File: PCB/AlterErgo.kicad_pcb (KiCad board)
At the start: 2 copper layers, 99 parts, among them J1 GS3, J2 SJ-43514, J3 GS3, SW0:10 SW_Push, SW0:11 SW_Push, SW0:12 SW_Push, SW0:7 SW_Push, SW0:8 SW_Push, SW0:9 SW_Push, SW1 SW_SPST, SW1:10 SW_Push, SW1:11 SW_Push, SW1:12 SW_Push, SW1:13 SW_Push, SW1:9 SW_Push, SW2:10 SW_Push, SW2:11 SW_Push, SW2:12 SW_Push, SW2:13 SW_Push, SW2:7 SW_Push, SW2:8 SW_Push, SW2:9 SW_Push, SW3:10 SW_Push, SW3:11 SW_Push, SW3:12 SW_Push, SW3:13 SW_Push, SW3:8 SW_Push, SW3:9 SW_Push, SW4:10 SW_Push, SW4:11 SW_Push, SW4:12 SW_Push, SW4:13 SW_Push, SW4:7 SW_Push, SW4:8 SW_Push, SW4:9 SW_Push, SW5:10 SW_Push, SW5:11 SW_Push, SW5:12 SW_Push, SW5:13 SW_Push, SW5:7 SW_Push, SW5:8 SW_Push, SW5:9 SW_Push, U1 Feather32u4Bluefruit, U2 MCP23018

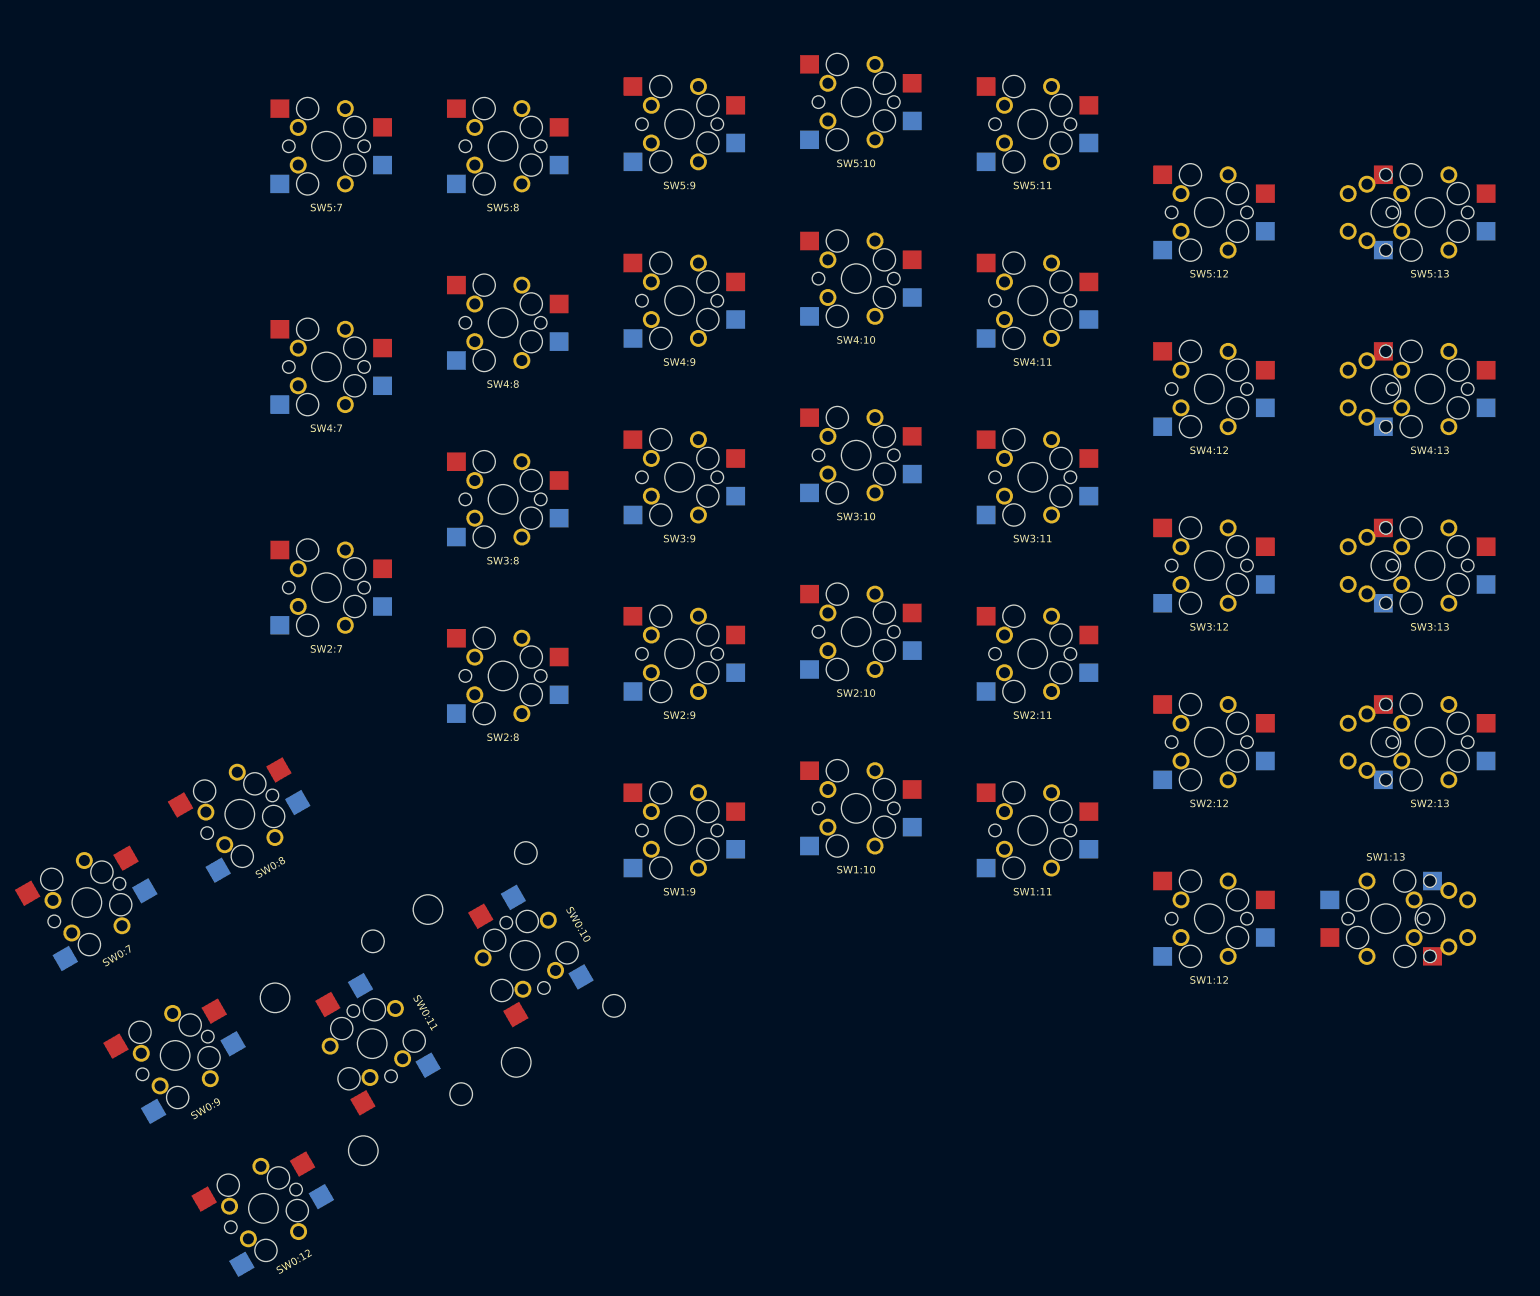
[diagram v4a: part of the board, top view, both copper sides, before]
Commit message: Actually use .75in for key spacing (d'oh!)
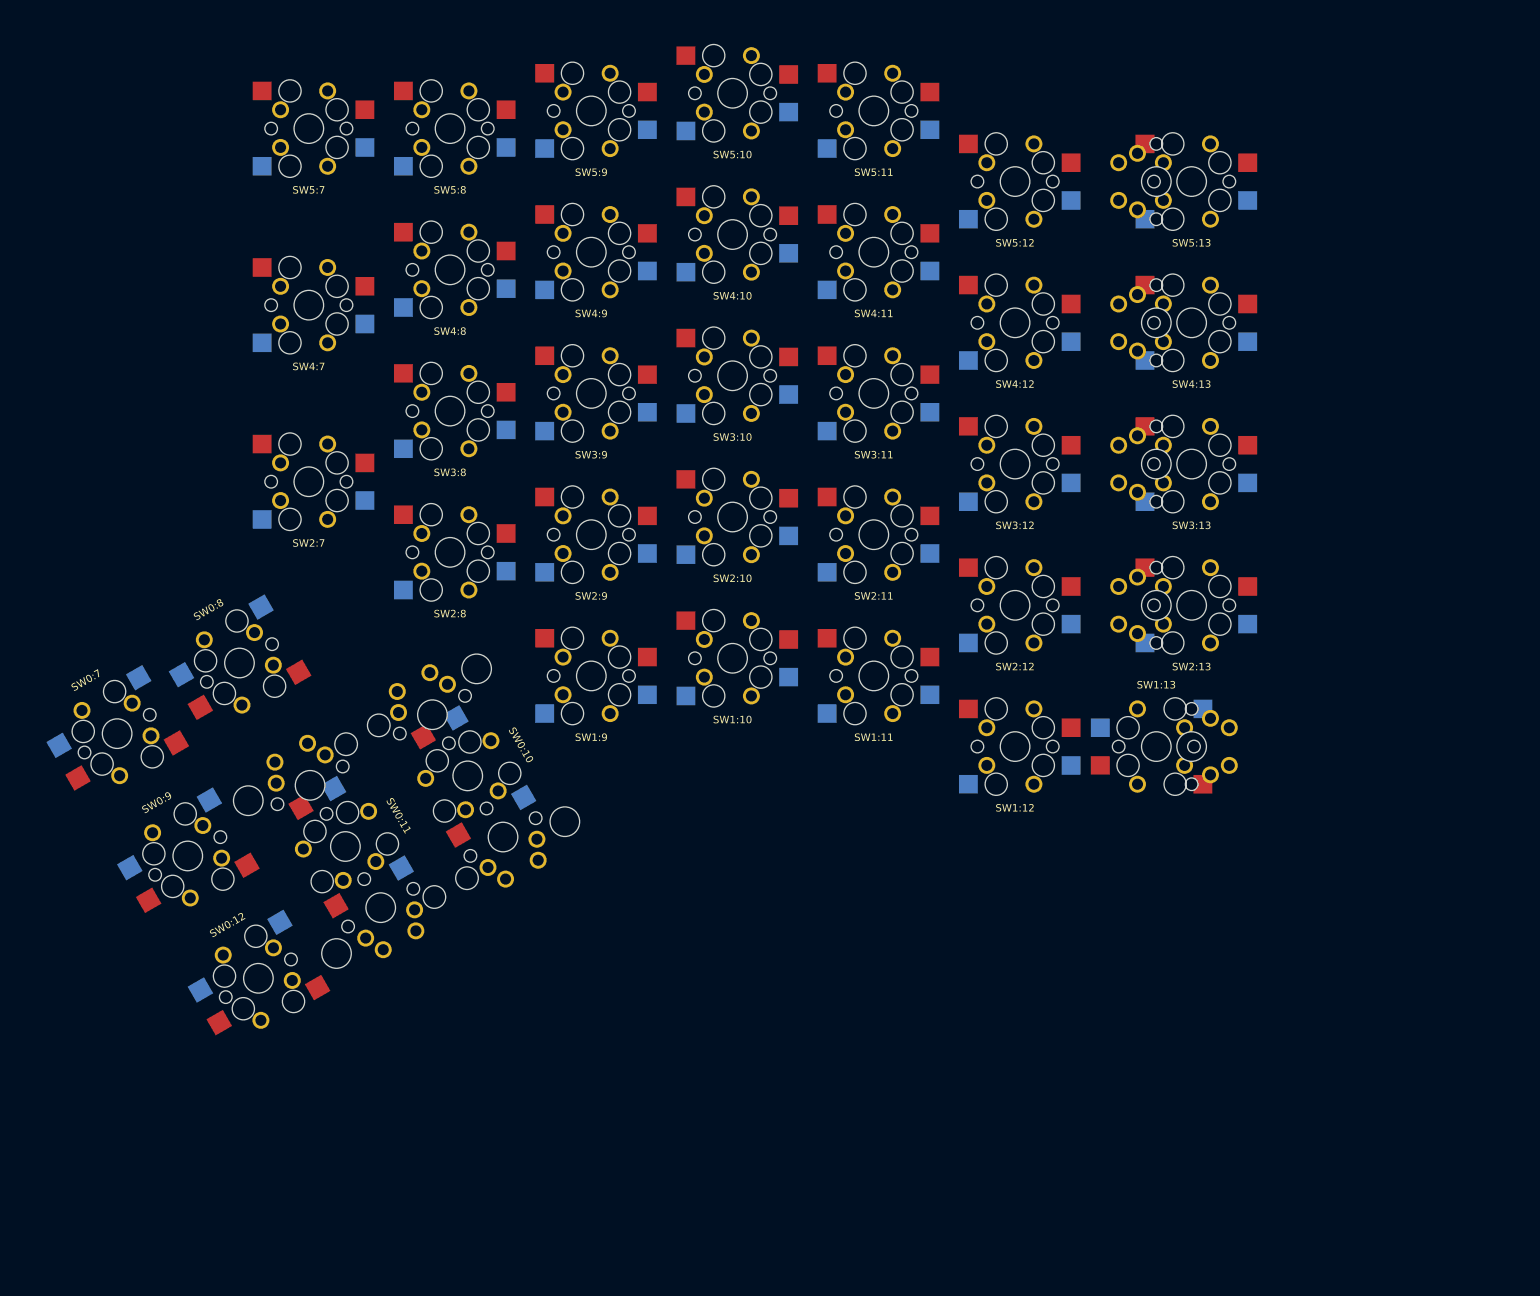
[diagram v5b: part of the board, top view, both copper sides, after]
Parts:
- added SW0:10: SW_Push, keyswitches:MX_reversible, F.Cu at (107.2, 152.7)
- added SW0:11: SW_Push, keyswitches:MX_reversible, F.Cu at (90.7, 162.2)
- added SW1:7: SW_Push, keyswitches:MX_reversible, F.Cu at (81.1, 145.7)
- added SW1:8: SW_Push, keyswitches:MX_reversible, F.Cu at (97.6, 136.2)
- moved ? 39.7 mm to (200.0, 140.5)
- moved SW1:13 38.7 mm to (195.3, 140.5)
- moved SW2:13 37.1 mm to (200.0, 121.4)
- moved ? 36.0 mm to (195.3, 121.4)
- moved SW1:12 35.0 mm to (176.2, 140.5)
- moved SW3:13 34.9 mm to (200.0, 102.4)
- moved ? 33.8 mm to (195.3, 102.4)
- moved SW4:13 33.4 mm to (200.0, 83.3)
- moved SW5:13 32.4 mm to (200.0, 64.3)
- moved ? 32.2 mm to (195.3, 83.3)
- moved SW2:12 32.0 mm to (176.2, 121.4)
- moved ? 31.2 mm to (195.3, 64.3)
- moved SW0:12 31.0 mm to (74.2, 171.7), turned to 210 degrees
- moved SW1:11 29.9 mm to (157.2, 131.0)
- moved SW3:12 29.6 mm to (176.2, 102.4)
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
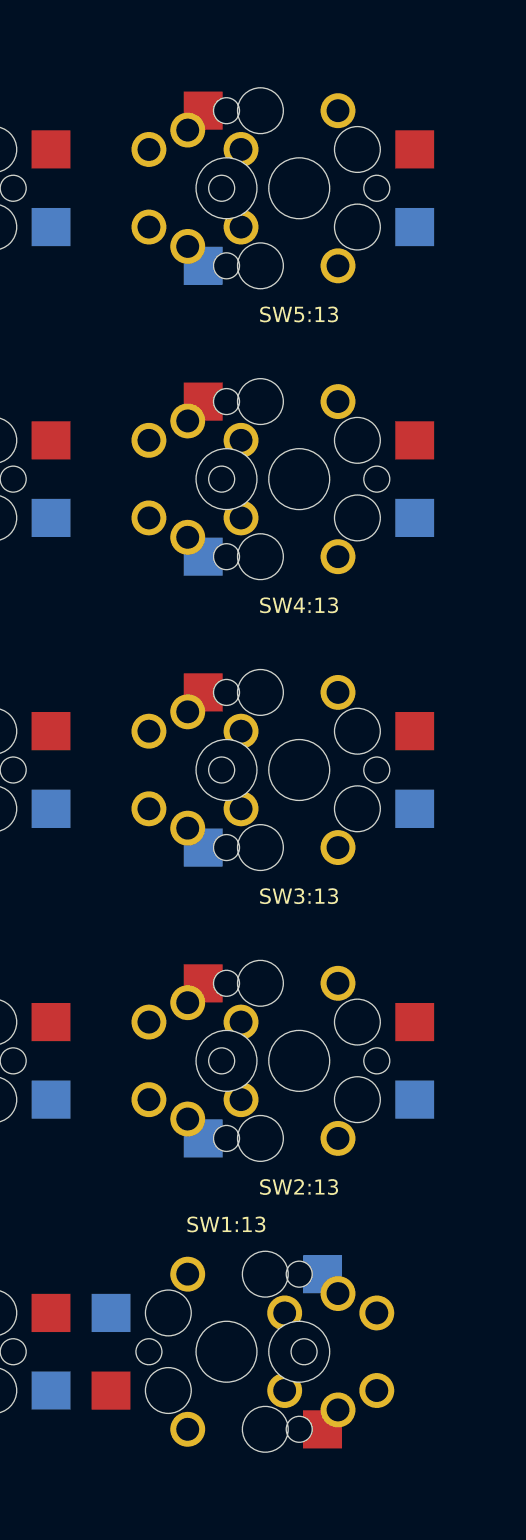
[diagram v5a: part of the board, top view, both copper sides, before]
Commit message: Avoid overlapping holes for switches that have alternate mounting options
Unfortunately this means that the outer column will *require* socket mounting for the default positions and soldering for the alternate positions, instead of allowing either method
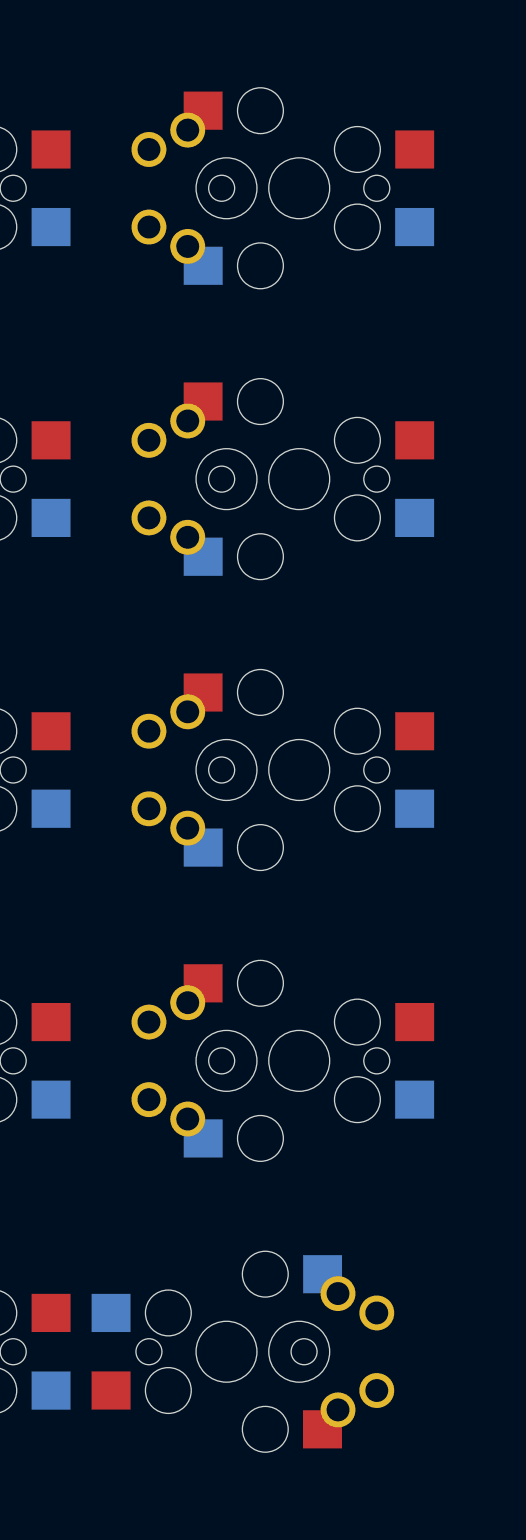
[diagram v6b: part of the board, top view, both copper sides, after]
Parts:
- ? (x5): footprint keyswitches:MX_reversible -> keyswitches:MX_reversible_minimal
- SW1:13, SW2:13, SW3:13, SW4:13, SW5:13: footprint keyswitches:Kailh_socket_optional_reversible -> keyswitches:Kailh_socket_reversible
- turned SW1:13 to 0 degrees
- turned SW2:13 to 180 degrees
- turned SW3:13 to 180 degrees
- turned SW4:13 to 180 degrees
- turned SW5:13 to 180 degrees
